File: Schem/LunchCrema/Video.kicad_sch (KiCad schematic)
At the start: 42 parts, among them IC1 MMPQ3904, J3 DE15_Socket_HighDensity_Mount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, U10 74HC139, U2 V9958, U3 74HC273, U8 74LVC1G19, Y1 HC-49/U-S21477270ABJB, Y2 CPPLC5-HT7PT

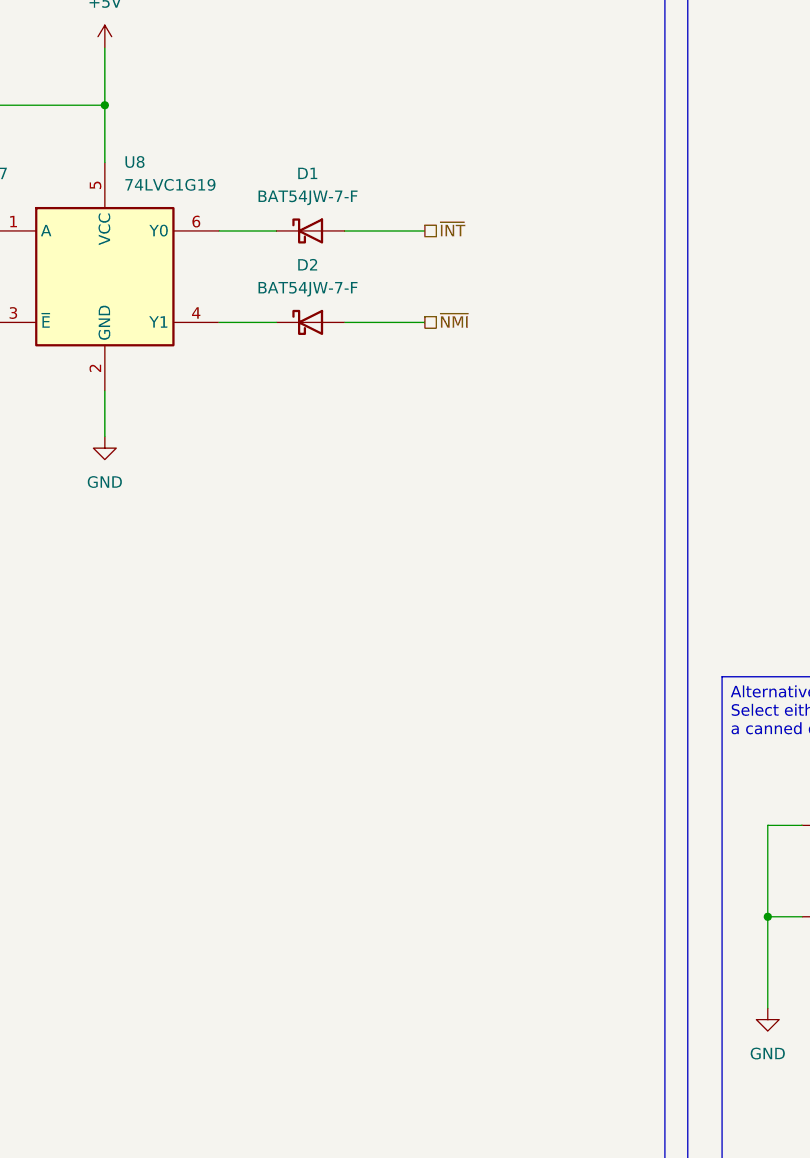
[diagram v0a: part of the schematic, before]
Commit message: Added both the Morning Joe and the Lunch Crema schematics, PCB, and KiCad library files.
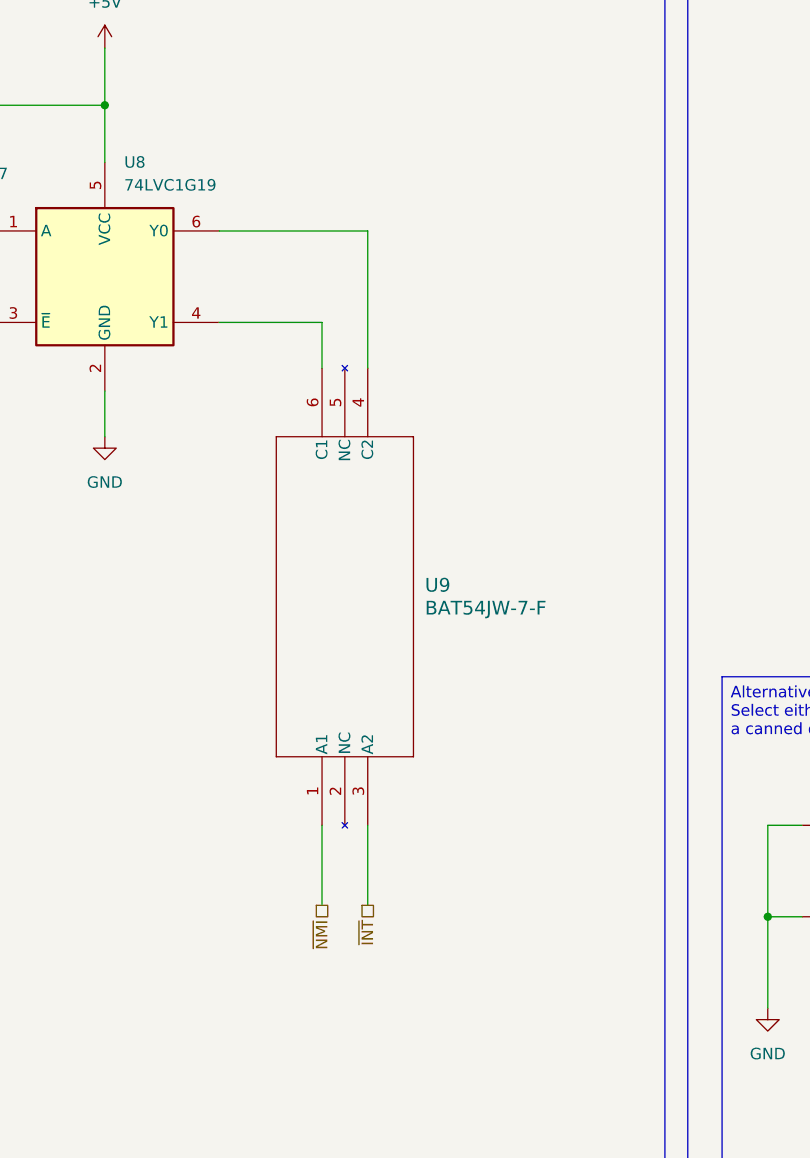
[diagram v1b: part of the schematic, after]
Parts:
- removed D1, D2: BAT54JW-7-F, Diode_SMD:D_SOD-323F, symbol Diode:BAT54J
- added U9: BAT54JW-7-F, Package_TO_SOT_SMD:SOT-363_SC-70-6, symbol 2026-06-14_23-32-30:BAT54JW-7-F
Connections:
- net ~{INT}: now also U9.3 (A2)
- net ~{NMI}: now also U9.1 (A1)
- net at U8.6 (Y0): now also U9.4 (C2)
- net at U8.4 (Y1): now also U9.6 (C1)
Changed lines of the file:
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@@
 	(wire
 		(pts
-			(xy 143.51 215.9) (xy 149.86 215.9)
+			(xy 143.51 215.9) (xy 154.94 215.9)
 		)
 		(stroke
@@
 	(wire
 		(pts
+			(xy 160.02 205.74) (xy 160.02 220.98)
+		)
+		(stroke
+			(width 0)
+			(type default)
+		)
+	)
+	(wire
+		(pts
 			(xy 68.58 78.74) (xy 78.74 78.74)
 		)
@@
 	(wire
 		(pts
+			(xy 154.94 215.9) (xy 154.94 220.98)
+		)
+		(stroke
+			(width 0)
+			(type default)
+		)
+	)
+	(wire
+		(pts
 			(xy 204.47 281.94) (xy 208.28 281.94)
 		)
@@
 	(wire
 		(pts
-			(xy 157.48 205.74) (xy 166.37 205.74)
+			(xy 160.02 271.78) (xy 160.02 280.67)
 		)
 		(stroke
@@
 	(wire
 		(pts
-			(xy 157.48 215.9) (xy 166.37 215.9)
+			(xy 154.94 271.78) (xy 154.94 280.67)
 		)
 		(stroke
@@
 	(wire
 		(pts
-			(xy 143.51 205.74) (xy 149.86 205.74)
+			(xy 143.51 205.74) (xy 160.02 205.74)
 		)
 		(stroke
@@
 	(hierarchical_label "~{NMI}"
 		(shape passive)
-		(at 166.37 215.9 0)
+		(at 154.94 280.67 270)
 		(effects
 			(font
 				(size 1.27 1.27)
 			)
-			(justify left)
+			(justify right)
 		)
 	)
@@
 	(hierarchical_label "~{INT}"
 		(shape passive)
-		(at 166.37 205.74 0)
+		(at 160.02 280.67 270)
 		(effects
 			(font
 				(size 1.27 1.27)
 			)
-			(justify left)
+			(justify right)
 		)
 	)
@@
 	)
 	(symbol
-		(lib_id "Diode:BAT54J")
-		(at 153.67 205.74 0)
-		(unit 1)
-		(body_style 1)
-		(exclude_from_sim no)
-		(in_bom yes)
-		(on_board yes)
-		(in_pos_files yes)
-		(dnp no)
-		(fields_autoplaced yes)
-		(property "Reference" "D1"
-			(at 153.3525 199.39 0)
-			(show_name no)
-			(do_not_autoplace no)
-			(effects
-				(font
-					(size 1.27 1.27)
-				)
-			)
-		)
-		(property "Value" "BAT54JW-7-F"
-			(at 153.3525 201.93 0)
-			(show_name no)
-			(do_not_autoplace no)
-			(effects
-				(font
-					(size 1.27 1.27)
-				)
-			)
-		)
-		(property "Footprint" "Diode_SMD:D_SOD-323F"
-			(at 153.67 210.185 0)
-			(hide yes)
-			(show_name no)
-			(do_not_autoplace no)
-			(effects
-				(font
-					(size 1.27 1.27)
-				)
-			)
-		)
-		(property "Datasheet" "https://assets.nexperia.com/documents/data-sheet/BAT54J.pdf"
-			(at 153.67 205.74 0)
-			(hide yes)
-			(show_name no)
-			(do_not_autoplace no)
-			(effects
-				(font
-					(size 1.27 1.27)
-				)
-			)
-		)
-		(property "Description" "30V 200mA Schottky diode, SOD-323F"
-			(at 153.67 205.74 0)
-			(hide yes)
-			(show_name no)
-			(do_not_autoplace no)
-			(effects
-				(font
-					(size 1.27 1.27)
-				)
-			)
-		)
-		(pin "2"
-		)
-		(pin "1"
-		)
-		(instances
-			(project "LunchCrema"
-				(path "/cd23574f-7a7d-4a14-add5-f302c6d915cb/2c30826b-ba26-488b-8dcd-4571fddacffc"
-					(reference "D1")
-					(unit 1)
-				)
-			)
-		)
-	)
-	(symbol
 		(lib_id "power:+5V")
 		(at 85.09 415.29 0)
@@
 	)
 	(symbol
-		(lib_id "Diode:BAT54J")
-		(at 153.67 215.9 0)
-		(unit 1)
-		(body_style 1)
-		(exclude_from_sim no)
-		(in_bom yes)
-		(on_board yes)
-		(in_pos_files yes)
-		(dnp no)
-		(fields_autoplaced yes)
-		(property "Reference" "D2"
-			(at 153.3525 209.55 0)
-			(show_name no)
-			(do_not_autoplace no)
-			(effects
-				(font
-					(size 1.27 1.27)
-				)
-			)
-		)
-		(property "Value" "BAT54JW-7-F"
-			(at 153.3525 212.09 0)
-			(show_name no)
-			(do_not_autoplace no)
-			(effects
-				(font
-					(size 1.27 1.27)
-				)
-			)
-		)
-		(property "Footprint" "Diode_SMD:D_SOD-323F"
-			(at 153.67 220.345 0)
-			(hide yes)
-			(show_name no)
-			(do_not_autoplace no)
-			(effects
-				(font
-					(size 1.27 1.27)
-				)
-			)
-		)
-		(property "Datasheet" "https://assets.nexperia.com/documents/data-sheet/BAT54J.pdf"
-			(at 153.67 215.9 0)
-			(hide yes)
-			(show_name no)
-			(do_not_autoplace no)
-			(effects
-				(font
-					(size 1.27 1.27)
-				)
-			)
-		)
-		(property "Description" "30V 200mA Schottky diode, SOD-323F"
-			(at 153.67 215.9 0)
-			(hide yes)
-			(show_name no)
-			(do_not_autoplace no)
-			(effects
-				(font
-					(size 1.27 1.27)
-				)
-			)
-		)
-		(pin "2"
-		)
-		(pin "1"
-		)
-		(instances
-			(project "LunchCrema"
-				(path "/cd23574f-7a7d-4a14-add5-f302c6d915cb/2c30826b-ba26-488b-8dcd-4571fddacffc"
-					(reference "D2")
-					(unit 1)
-				)
-			)
-		)
-	)
-	(symbol
 		(lib_id "Device:R")
 		(at 303.53 213.36 180)
@@
 				)
 			)
+		)
+	)
+	(symbol
+		(lib_id "2026-06-14_23-32-30:BAT54JW-7-F")
+		(at 154.94 271.78 90)
+		(unit 1)
+		(body_style 1)
+		(exclude_from_sim no)
+		(in_bom yes)
+		(on_board yes)
+		(in_pos_files yes)
+		(dnp no)
+		(fields_autoplaced yes)
+		(property "Reference" "U9"
+			(at 166.37 245.1099 90)
+			(show_name no)
+			(do_not_autoplace no)
+			(effects
+				(font
+					(size 1.524 1.524)
+				)
+				(justify right)
+			)
+		)
+		(property "Value" "BAT54JW-7-F"
+			(at 166.37 247.6499 90)
+			(show_name no)
+			(do_not_autoplace no)
+			(effects
+				(font
+					(size 1.524 1.524)
+				)
+				(justify right)
+			)
+		)
+		(property "Footprint" "Package_TO_SOT_SMD:SOT-363_SC-70-6"
+			(at 154.94 271.78 0)
+			(hide yes)
+			(show_name no)
+			(do_not_autoplace no)
+			(effects
+				(font
+					(size 1.27 1.27)
+					(italic yes)
+				)
+			)
+		)
+		(property "Datasheet" "BAT54JW-7-F"
+			(at 154.94 271.78 0)
+			(hide yes)
+			(show_name no)
+			(do_not_autoplace no)
+			(effects
+				(font
+					(size 1.27 1.27)
+					(italic yes)
+				)
+			)
+		)
+		(property "Description" ""
+			(at 154.94 271.78 0)
+			(hide yes)
+			(show_name no)
+			(do_not_autoplace no)
+			(effects
+				(font
+					(size 1.27 1.27)
+				)
+			)
+		)
+		(property "MANUFACTURER_PART_NUMBER" "BAT54JW-7-F"
+			(at 154.94 271.78 90)
+			(hide yes)
+			(show_name no)
+			(do_not_autoplace no)
+			(effects
+				(font
+					(size 1.27 1.27)
+				)
+			)
+		)
+		(pin "1"
+		)
+		(pin "4"
+		)
+		(pin "2"
+		)
+		(pin "5"
+		)
+		(pin "6"
+		)
+		(pin "3"
+		)
+		(instances
+			(project "LunchCrema"
+				(path "/cd23574f-7a7d-4a14-add5-f302c6d915cb/2c30826b-ba26-488b-8dcd-4571fddacffc"
+					(reference "U9")
+					(unit 1)
+				)
+			)

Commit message: Review and Fixes
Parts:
- removed R6: 4k7, Resistor_SMD:R_0603_1608Metric, symbol Device:R
- added R20: 4k7, Resistor_SMD:R_0603_1608Metric, symbol Device:R
- R7, Y2: now not fitted; now left out of the parts list
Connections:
- net +5V: now also U2.27 (~{HRESET}), U2.4 (~{VRESET}), R20.2
- net at U2.3 (~{DLCLK}): now also R20.1
- no-connect marks 34 -> 33

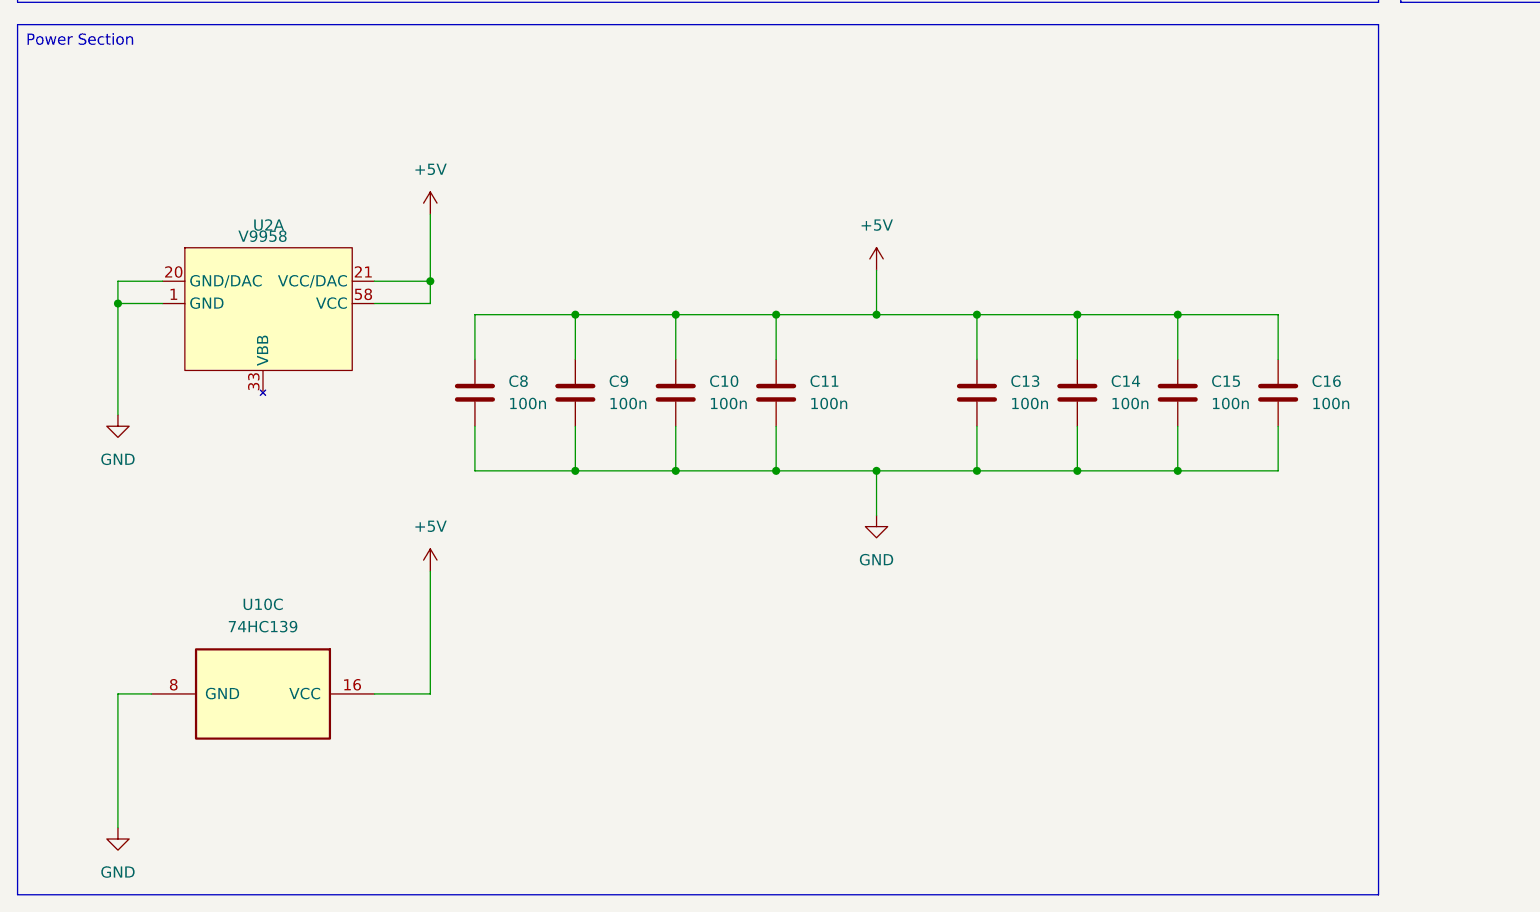
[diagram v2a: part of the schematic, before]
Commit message: Added bulk caps and fixed up the part numbers
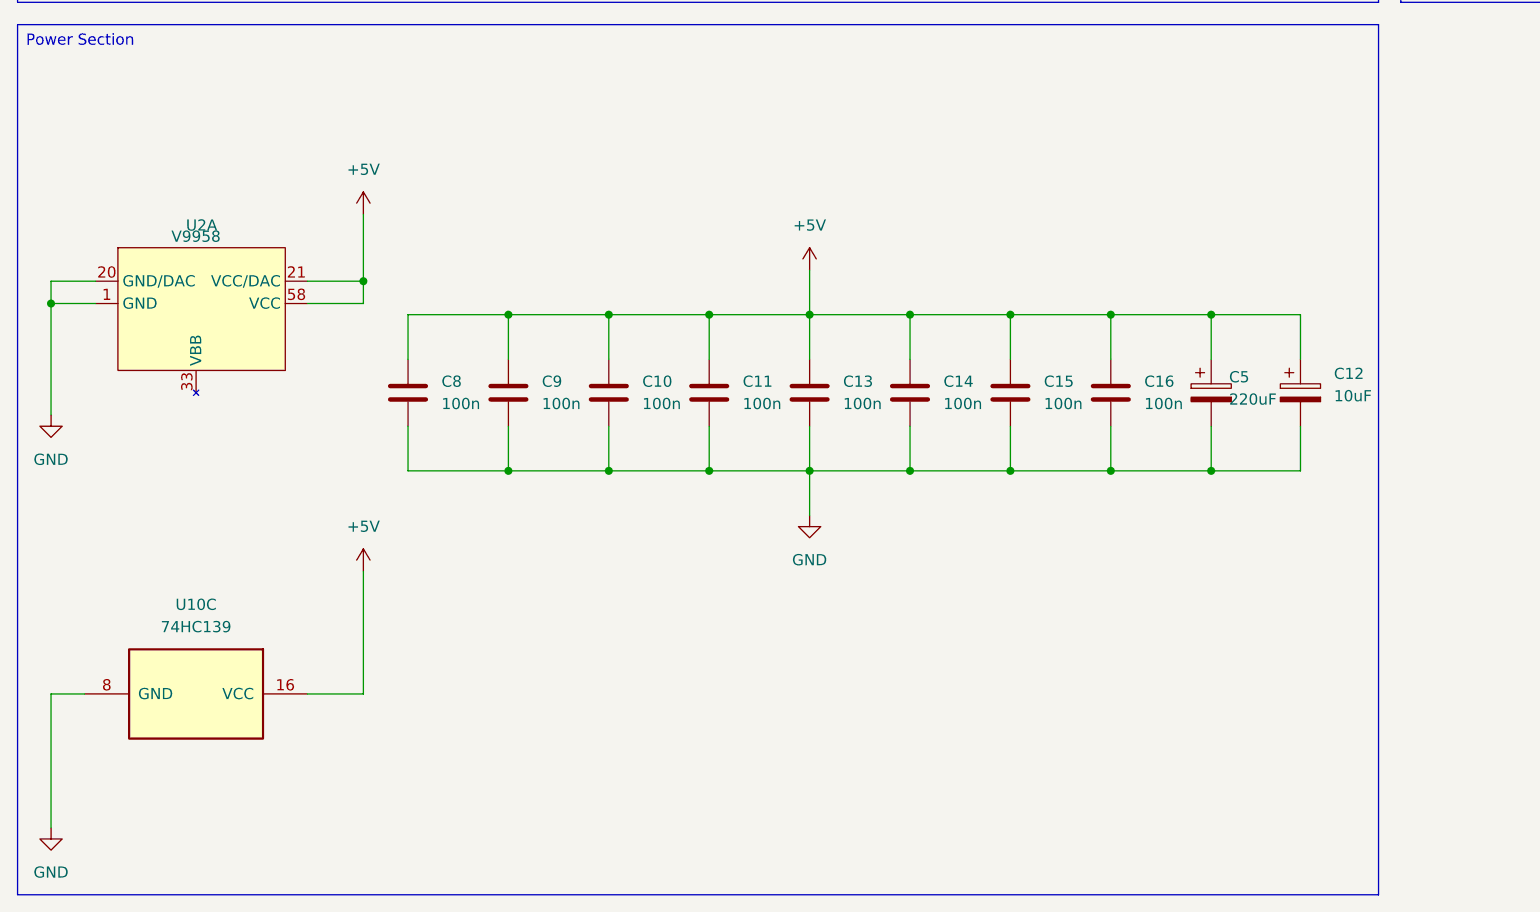
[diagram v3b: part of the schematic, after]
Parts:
- added C12: 10uF, Capacitor_THT:CP_Radial_D5.0mm_P2.50mm, symbol Device:C_Polarized
- added C5: 220uF, Capacitor_THT:CP_Radial_D6.3mm_P2.50mm, symbol Device:C_Polarized
- C2, C3, C4: MANUFACTURER_PART_NUMBER 25YXJ220M6.3X11 -> 25YXJ220M6.3X11s
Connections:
- net +5V: now also C12.1, C5.1
- net GND: now also C12.2, C5.2
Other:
- moved on the sheet: C10, C11, C13, C14, C15, C16, C8, C9, U10C, U2A
